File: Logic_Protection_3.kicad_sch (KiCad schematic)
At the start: 15 parts

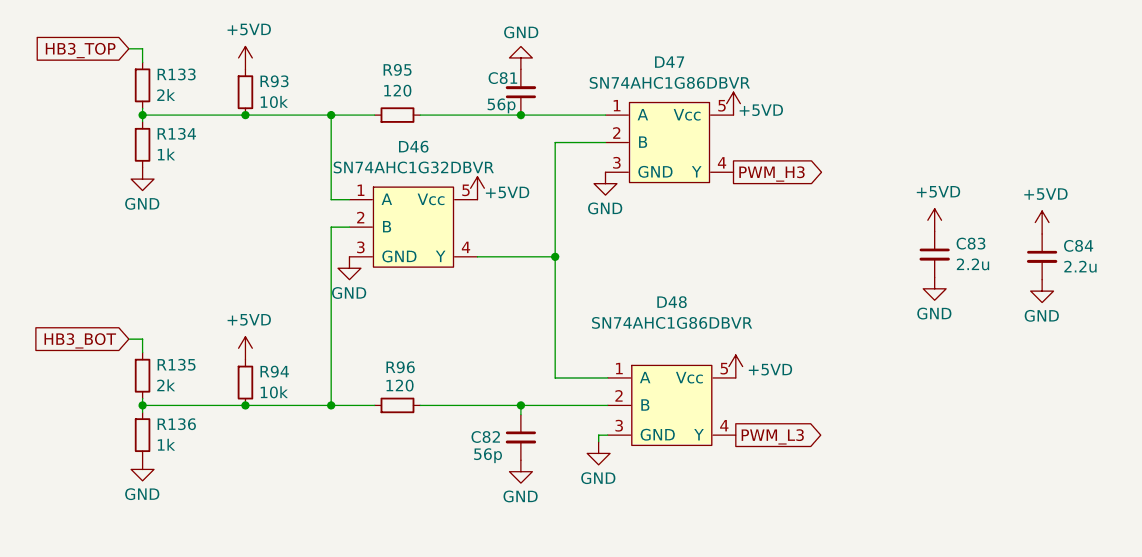
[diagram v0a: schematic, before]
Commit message: Всё влезло, осталься компаратор на NTC
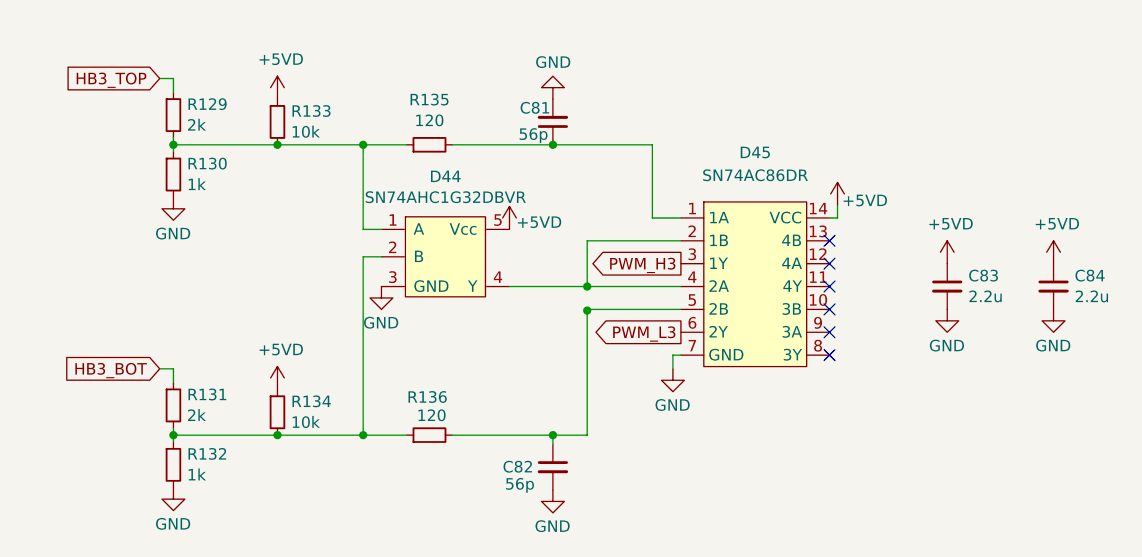
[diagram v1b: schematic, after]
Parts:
- removed D46: SN74AHC1G32DBVR, Package_TO_SOT_SMD:SOT-23-5_HandSoldering, symbol Logic:SN74AHC1G86DBVR
- removed D47, D48: SN74AHC1G86DBVR, Package_TO_SOT_SMD:SOT-23-5_HandSoldering, symbol Logic:SN74AHC1G86DBVR
- removed R93, R94: 10k, Resistor_SMD:R_0805_2012Metric_Pad1.20x1.40mm_HandSolder, symbol Device:R_Small
- removed R95, R96: 120, Resistor_SMD:R_0805_2012Metric_Pad1.20x1.40mm_HandSolder, symbol Device:R_Small
- added D44: SN74AHC1G32DBVR, Package_TO_SOT_SMD:SOT-23-5_HandSoldering, symbol Logic:SN74AHC1G86DBVR
- added D45: SN74AC86DR, Package_SO:SOIC-14_3.9x8.7mm_P1.27mm, symbol Logic_My:SN74AC86DR
- added R129, R131: 2k, Resistor_SMD:R_0805_2012Metric_Pad1.20x1.40mm_HandSolder, symbol Device:R_Small
- added R130, R132: 1k, Resistor_SMD:R_0805_2012Metric_Pad1.20x1.40mm_HandSolder, symbol Device:R_Small
- R133: value 2k -> 10k
- R134: value 1k -> 10k
- R135: value 2k -> 120
- R136: value 1k -> 120
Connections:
- net +5VD: now also R133.1, R134.1, D44.5 (Vcc), D45.14 (VCC)
- net GND: now also D44.3 (GND), D45.7 (GND), R130.2, R132.2; no longer R134.2, R136.2
- net HB3_BOT: now also R131.1; no longer R135.1
- net HB3_TOP: now also R129.1; no longer R133.1
- net PWM_H3: now also D45.3 (1Y)
- net PWM_L3: now also D45.6 (2Y)
- net at R136.1: now also R134.2, D44.2 (B), R131.2, R132.1; no longer R135.2
- net at R133.2: now also R135.1, D44.1 (A), R129.2, R130.1; no longer R134.1
- net at C81.1: now also R135.2, D45.1 (1A)
- net at C82.1: now also R136.2, D45.5 (2B)
- new net: D44.4 (Y), D45.2 (1B), D45.4 (2A)
- no-connect marks 0 -> 6

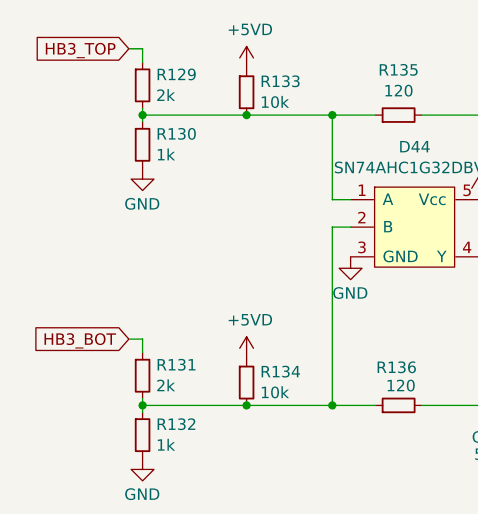
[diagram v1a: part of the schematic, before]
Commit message: Исправил ошибки, добавил резисторы в затвор, ревизия 2.0
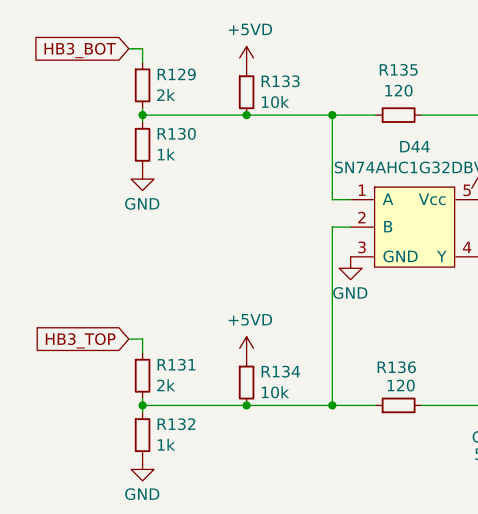
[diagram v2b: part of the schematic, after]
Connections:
- net HB3_BOT: now also R129.1; no longer R131.1
- net HB3_TOP: now also R131.1; no longer R129.1
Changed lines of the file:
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@@
     )
   )
-  (global_label "HB3_TOP" (shape input) (at 101.6 77.724 180) (fields_autoplaced)
+  (global_label "HB3_TOP" (shape input) (at 101.6 109.982 180) (fields_autoplaced)
+    (effects (font (size 1.27 1.27)) (justify right))
+    (property "Intersheet References" "${INTERSHEET_REFS}" (id 0) (at 90.8412 109.9026 0)
+      (effects (font (size 1.27 1.27)) (justify right) hide)
+    )
+  )
+  (global_label "HB3_BOT" (shape input) (at 101.6 77.724 180) (fields_autoplaced)
     (effects (font (size 1.27 1.27)) (justify right))
     (property "Intersheet References" "${INTERSHEET_REFS}" (id 0) (at 90.8412 77.6446 0)
       (effects (font (size 1.27 1.27)) (justify right) hide)
     )
-  )
-  (global_label "HB3_BOT" (shape input) (at 101.6 109.982 180) (fields_autoplaced)
-    (effects (font (size 1.27 1.27)) (justify right))
-    (property "Intersheet References" "${INTERSHEET_REFS}" (id 0) (at 90.8412 109.9026 0)
-      (effects (font (size 1.27 1.27)) (justify right) hide)
-    )

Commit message: Версия для резонита REV2.1
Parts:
- removed C81, C82: 56p, Capacitor_SMD:C_0805_2012Metric_Pad1.18x1.45mm_HandSolder, symbol Device:C_Small
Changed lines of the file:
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@@
   (junction (at 103.124 85.09) (diameter 0) (color 0 0 0 0)
   )
-  (junction (at 145.288 85.09) (diameter 0) (color 0 0 0 0)
-  )
   (junction (at 124.206 117.348) (diameter 0) (color 0 0 0 0)
   )
@@
   )
   (junction (at 149.098 100.838) (diameter 0) (color 0 0 0 0)
-  )
-  (junction (at 145.288 117.348) (diameter 0) (color 0 0 0 0)
   )
   (junction (at 124.206 85.09) (diameter 0) (color 0 0 0 0)
@@
     (stroke (width 0) (type default) (color 0 0 0 0))
   )
-  (wire (pts (xy 134.112 117.348) (xy 145.288 117.348))
-    (stroke (width 0) (type default) (color 0 0 0 0))
-  )
   (wire (pts (xy 124.206 94.488) (xy 126.238 94.488))
     (stroke (width 0) (type default) (color 0 0 0 0))
@@
     (stroke (width 0) (type default) (color 0 0 0 0))
   )
-  (wire (pts (xy 149.098 117.348) (xy 145.288 117.348))
-    (stroke (width 0) (type default) (color 0 0 0 0))
-  )
-  (wire (pts (xy 134.112 85.09) (xy 145.288 85.09))
+  (wire (pts (xy 134.112 117.348) (xy 149.098 117.348))
+    (stroke (width 0) (type default) (color 0 0 0 0))
+  )
+  (wire (pts (xy 134.112 85.09) (xy 156.337 85.09))
     (stroke (width 0) (type default) (color 0 0 0 0))
   )
@@
     (stroke (width 0) (type default) (color 0 0 0 0))
   )
-  (wire (pts (xy 145.288 85.09) (xy 156.337 85.09))
-    (stroke (width 0) (type default) (color 0 0 0 0))
-  )
   (wire (pts (xy 159.512 103.378) (xy 149.098 103.378))
-    (stroke (width 0) (type default) (color 0 0 0 0))
-  )
-  (wire (pts (xy 145.288 117.348) (xy 145.288 118.364))
     (stroke (width 0) (type default) (color 0 0 0 0))
   )
@@
     )
   )
-  (symbol (lib_id "power:GND") (at 145.288 80.01 180) (unit 1)
-    (in_bom yes) (on_board yes)
-    (property "Reference" "#PWR064" (id 0) (at 145.288 73.66 0)
-      (effects (font (size 1.27 1.27)) hide)
-    )
-    (property "Value" "GND" (id 1) (at 147.32 75.946 0)
-      (effects (font (size 1.27 1.27)) (justify left))
-    )
-    (property "Footprint" "" (id 2) (at 145.288 80.01 0)
-      (effects (font (size 1.27 1.27)) hide)
-    )
-    (property "Datasheet" "" (id 3) (at 145.288 80.01 0)
-      (effects (font (size 1.27 1.27)) hide)
-    )
-    (pin "1")
-  )
   (symbol (lib_id "power:GND") (at 189.103 103.378 0) (unit 1)
     (in_bom yes) (on_board yes)
@@
     )
     (property "Datasheet" "~" (id 3) (at 114.681 82.55 0)
-      (effects (font (size 1.27 1.27)) hide)
-    )
-    (pin "1")
-    (pin "2")
-  )
-  (symbol (lib_id "Device:C_Small") (at 145.288 120.904 0) (unit 1)
-    (in_bom yes) (on_board yes)
-    (property "Reference" "C82" (id 0) (at 139.7 120.904 0)
-      (effects (font (size 1.27 1.27)) (justify left))
-    )
-    (property "Value" "56p" (id 1) (at 139.954 122.809 0)
-      (effects (font (size 1.27 1.27)) (justify left))
-    )
-    (property "Footprint" "Capacitor_SMD:C_0805_2012Metric_Pad1.18x1.45mm_HandSolder" (id 2) (at 145.288 120.904 0)
-      (effects (font (size 1.27 1.27)) hide)
-    )
-    (property "Datasheet" "~" (id 3) (at 145.288 120.904 0)
       (effects (font (size 1.27 1.27)) hide)
     )
@@
     (pin "2")
   )
-  (symbol (lib_id "Device:C_Small") (at 145.288 82.55 180) (unit 1)
-    (in_bom yes) (on_board yes)
-    (property "Reference" "C81" (id 0) (at 145.034 81.026 0)
-      (effects (font (size 1.27 1.27)) (justify left))
-    )
-    (property "Value" "56p" (id 1) (at 144.78 83.947 0)
-      (effects (font (size 1.27 1.27)) (justify left))
-    )
-    (property "Footprint" "Capacitor_SMD:C_0805_2012Metric_Pad1.18x1.45mm_HandSolder" (id 2) (at 145.288 82.55 0)
-      (effects (font (size 1.27 1.27)) hide)
-    )
-    (property "Datasheet" "~" (id 3) (at 145.288 82.55 0)
-      (effects (font (size 1.27 1.27)) hide)
-    )
-    (pin "1")
-    (pin "2")
-  )
   (symbol (lib_id "power:+5VD") (at 200.914 98.298 0) (unit 1)
     (in_bom yes) (on_board yes)
@@
       (effects (font (size 1.27 1.27)) hide)
     )
-    (pin "1")
-  )
-  (symbol (lib_id "power:GND") (at 145.288 123.444 0) (unit 1)
-    (in_bom yes) (on_board yes)
-    (property "Reference" "#PWR067" (id 0) (at 145.288 129.794 0)
-      (effects (font (size 1.27 1.27)) hide)
-    )
-    (property "Value" "GND" (id 1) (at 143.256 127.508 0)
-      (effects (font (size 1.27 1.27)) (justify left))
-    )
-    (property "Footprint" "" (id 2) (at 145.288 123.444 0)
-      (effects (font (size 1.27 1.27)) hide)
-    )
-    (property "Datasheet" "" (id 3) (at 145.288 123.444 0)
-      (effects (font (size 1.27 1.27)) hide)
-    )
